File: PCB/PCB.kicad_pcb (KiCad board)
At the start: 2 copper layers, 101.6 x 39.7 mm, 38 parts, among them J1 USB_C_Receptacle_USB2.0, SW1 SW_Push, U1 ATmega32U4-AU, Y1 16MHz

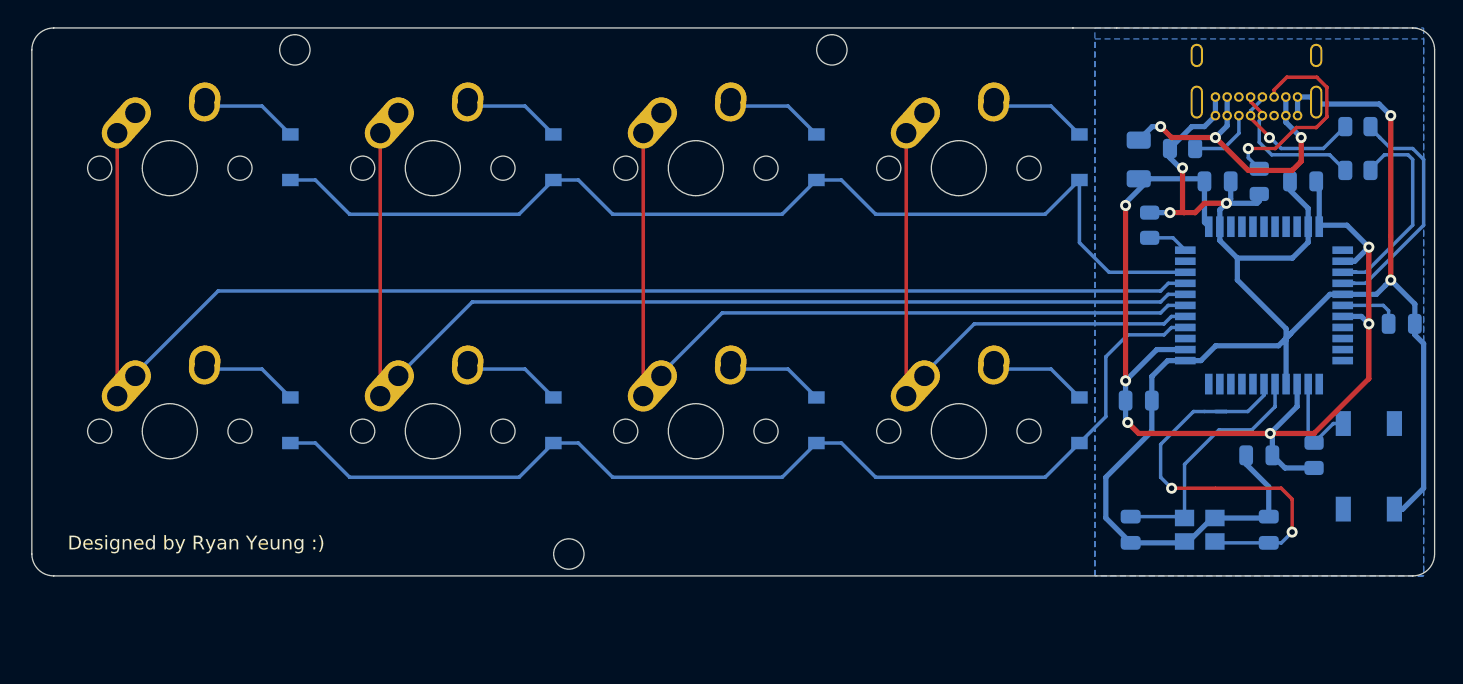
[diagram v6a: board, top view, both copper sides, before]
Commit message: replaced mc with ATMEGA32u2
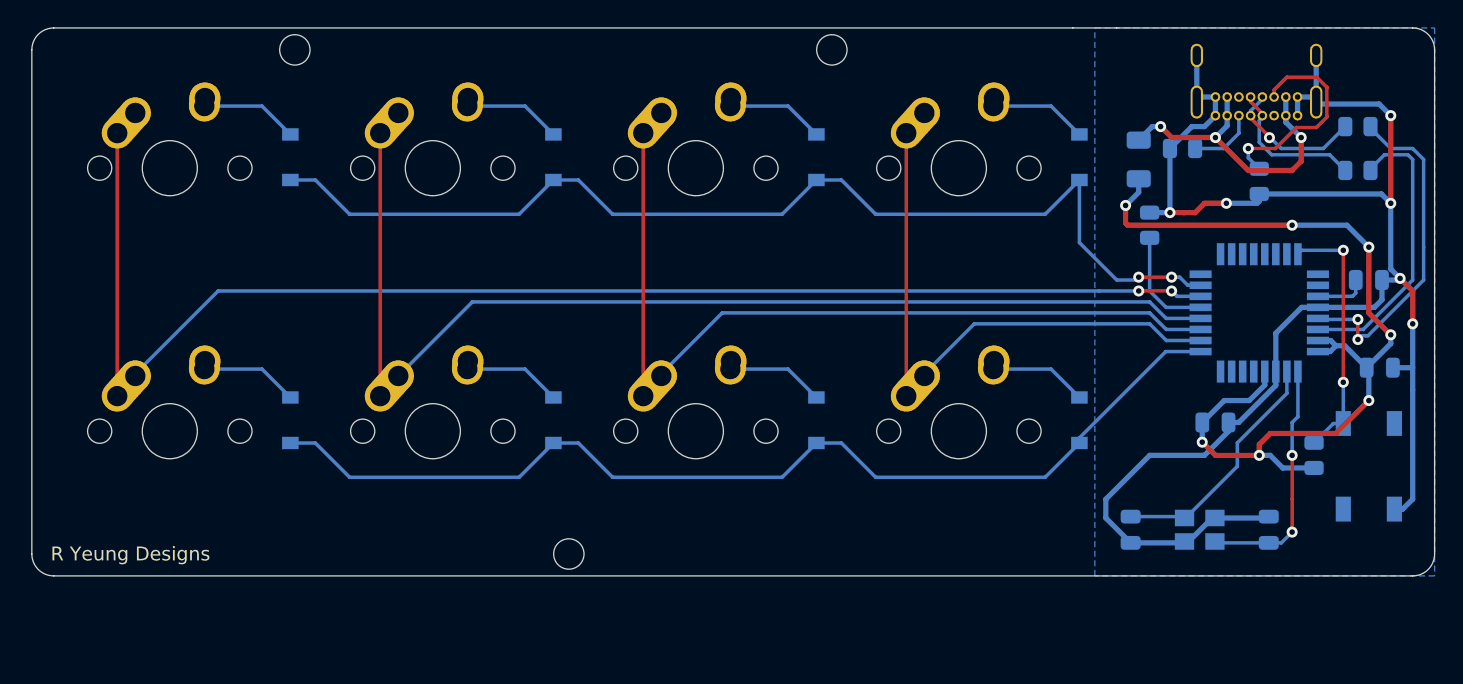
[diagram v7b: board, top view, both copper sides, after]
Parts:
- removed C1, C2: 0.1 uF, Capacitor_SMD:C_0805_2012Metric
- U1: value ATmega32U4-AU -> ATmega32U2-AU; footprint Package_QFP:TQFP-44_10x10mm_P0.8mm -> Package_QFP:TQFP-32_7x7mm_P0.8mm
- moved C6 17.9 mm to (218.3, 92.9)
- moved C5 3.97 mm to (206.4, 96.8), turned to 0 degrees
- moved C7 3.97 mm to (217.5, 86.5)
- moved U1 0.64 mm to (209.6, 88.9), turned to 90 degrees
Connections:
- U1 pad 1: Net-(U1-Pad1) -> Net-(C3-Pad1)
- U1 pad 10: Net-(U1-Pad10) -> COL3
- U1 pad 11: Net-(U1-Pad11) -> COL2
- U1 pad 12: Net-(U1-Pad12) -> COL1
- U1 pad 13: Net-(R3-Pad2) -> Net-(R4-Pad2)
- U1 pad 14: +5V -> COL0
- U1 pad 15: GND -> ROW0
- U1 pad 16: Net-(C4-Pad1) -> Net-(U1-Pad16)
- U1 pad 17: Net-(C3-Pad1) -> Net-(U1-Pad17)
- U1 pad 2: +5V -> Net-(C4-Pad1)
- U1 pad 23: GND -> Net-(U1-Pad23)
- U1 pad 24: +5V -> Net-(R3-Pad2)
- U1 pad 26: ROW1 -> Net-(U1-Pad26)
- U1 pad 27: COL3 -> Net-(C7-Pad1)
- U1 pad 28: COL2 -> GND
- U1 pad 29: COL1 -> Net-(R2-Pad1)
- U1 pad 3: Net-(R1-Pad1) -> GND
- U1 pad 30: COL0 -> Net-(R1-Pad1)
- U1 pad 31: ROW0 -> +5V
- U1 pad 32: Net-(U1-Pad32) -> +5V
- U1 pad 4: Net-(R2-Pad1) -> +5V
- U1 pad 5: GND -> Net-(U1-Pad5)
- U1 pad 6: Net-(C7-Pad1) -> Net-(U1-Pad6)
- U1 pad 7: +5V -> Net-(U1-Pad7)
- U1 pad 9: Net-(U1-Pad9) -> ROW1
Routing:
- net +5V: track 81.7 -> 67.5 mm, vias 6 -> 7
- net Net-(C3-Pad1): track 31.5 -> 17.8 mm
- net GND: track 136.7 -> 123.0 mm, vias 5 -> 6
- net Net-(R3-Pad2): track 7.24 -> 19.4 mm, vias 0 -> 2
- net Net-(R2-Pad1): track 18.1 -> 24.6 mm, vias 0 -> 2
- net Net-(R4-Pad2): track 2.95 -> 8.03 mm
- net Net-(R1-Pad1): track 16.0 -> 20.8 mm
- net ROW1: track 77.0 -> 75.1 mm
- net ROW0: track 76.4 -> 78.2 mm, vias 0 -> 2
- net COL3: track 41.8 -> 43.2 mm
- net COL2: track 61.7 -> 63.1 mm
- net COL1: track 78.5 -> 79.9 mm
- net COL0: track 100.0 -> 101.0 mm, vias 0 -> 2
- net Net-(C7-Pad1): track 4.59 -> 3.78 mm
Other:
- board text added: "R Yeung Designs"
- board text removed: "Designed by Ryan Yeung :)"

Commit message: added firmware
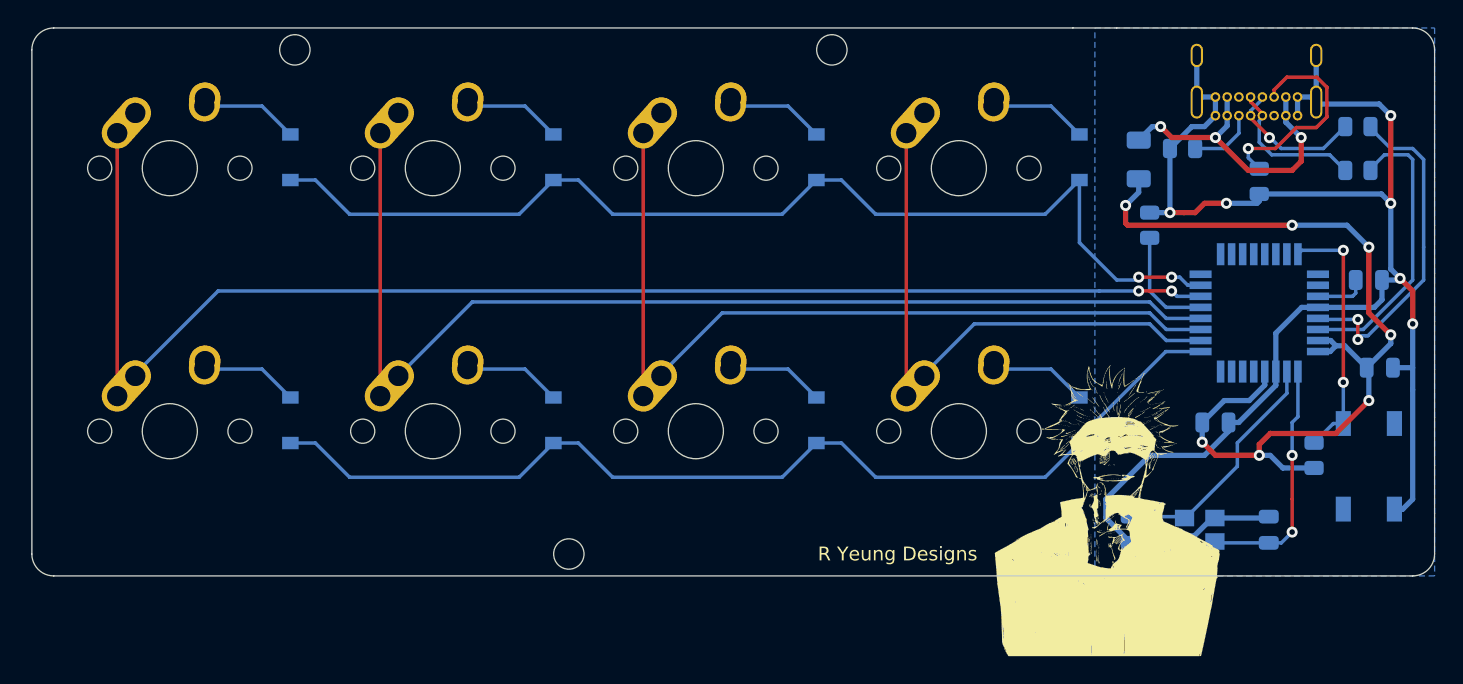
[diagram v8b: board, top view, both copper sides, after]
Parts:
- added G***: LOGO, gojo:gojo, F.Cu at (198.4, 103.2)
